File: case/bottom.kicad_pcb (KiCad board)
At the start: 2 copper layers, 135 x 93.7 mm, 5 parts

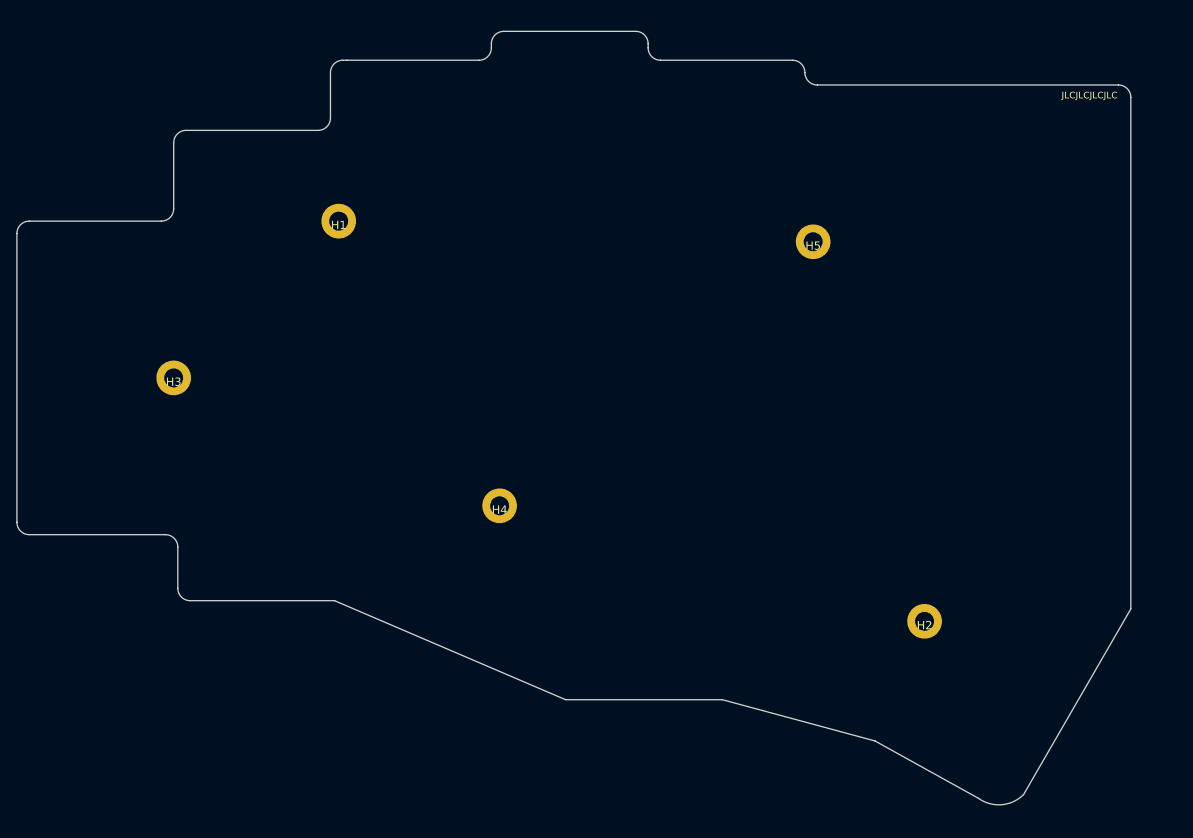
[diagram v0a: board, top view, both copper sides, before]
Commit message: update breakaway design to satisfy jlcpcb
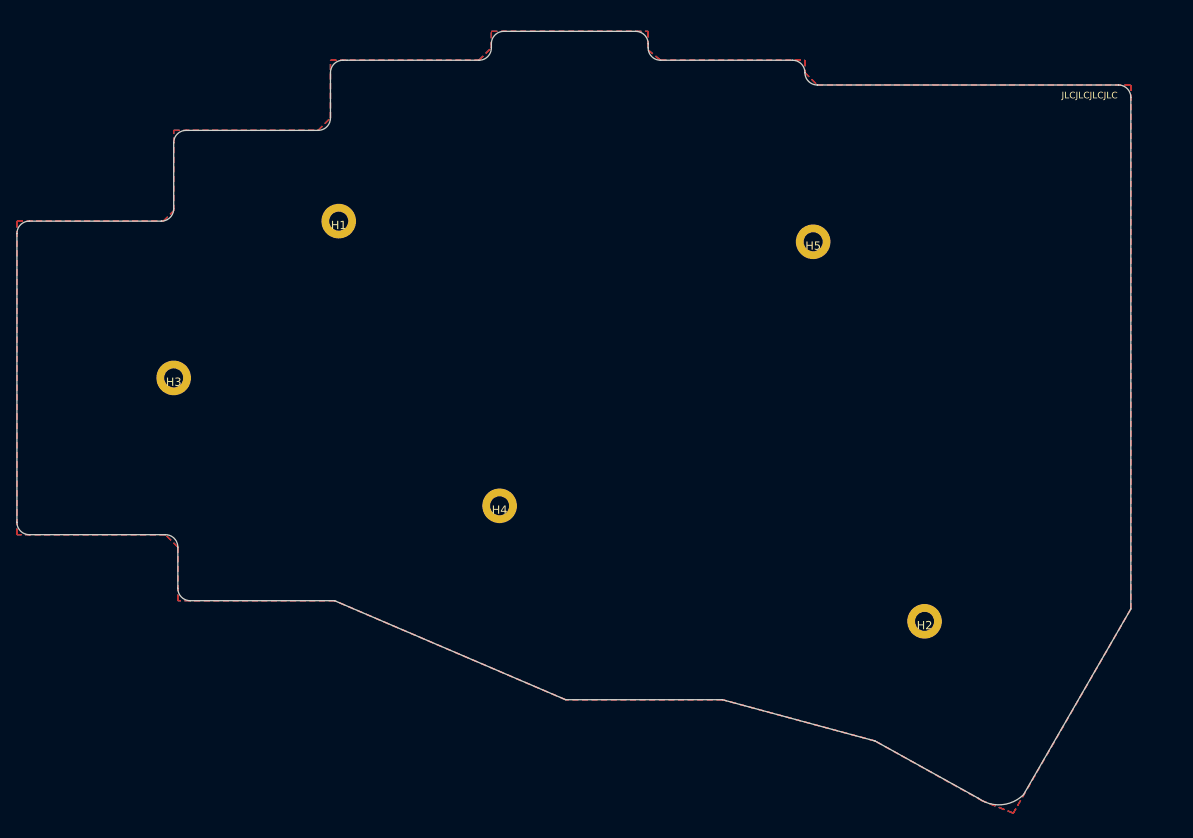
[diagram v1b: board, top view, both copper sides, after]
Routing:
- added copper zone on B.Cu, net (none)
- added copper zone on F.Cu, net (none)
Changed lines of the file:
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@@
     (effects (font (size 0.8 0.8) (thickness 0.15)))
   )
+  (zone (net 0) (net_name "") (layers F&B.Cu) (hatch edge 0.508)
+    (connect_pads (clearance 0.508))
+    (min_thickness 0.254) (filled_areas_thickness no)
+    (fill yes (thermal_gap 0.508) (thermal_bridge_width 0.508))
+    (polygon
+      (pts
+        (xy 145 53.75)
+        (xy 146.5 55)
+        (xy 164 55)
+        (xy 164 56.5)
+        (xy 165.5 58)
+        (xy 203.5 58)
+        (xy 203.5 121.5)
+        (xy 189.25 146.25)
+        (xy 185.5 144.75)
+        (xy 172.5 137.5)
+        (xy 154 132.5)
+        (xy 135 132.5)
+        (xy 107 120.5)
+        (xy 88 120.5)
+        (xy 88 114)
+        (xy 86.5 112.5)
+        (xy 68.5 112.5)
+        (xy 68.5 74.5)
+        (xy 86.25 74.5)
+        (xy 87.5 73.25)
+        (xy 87.5 63.5)
+        (xy 105 63.5)
+        (xy 106.5 62)
+        (xy 106.5 55)
+        (xy 124.5 55)
+        (xy 126 53.5)
+        (xy 126 51.5)
+        (xy 145 51.5)
+      )
+    )
+  )
+  (zone (net 0) (net_name "") (layer "F.Cu") (hatch edge 0.508)
+    (connect_pads (clearance 0.508))
+    (min_thickness 0.254) (filled_areas_thickness no)
+    (fill yes (thermal_gap 0.508) (thermal_bridge_width 0.508))
+    (polygon
+      (pts
+        (xy 145 53.75)
+        (xy 146.5 55)
+        (xy 164 55)
+        (xy 164 56.5)
+        (xy 165.5 58)
+        (xy 203.5 58)
+        (xy 203.5 121.5)
+        (xy 189.466207 145.874483)
+        (xy 189.25 146.25)
+        (xy 185.5 144.75)
+        (xy 172.5 137.5)
+        (xy 154 132.5)
+        (xy 135 132.5)
+        (xy 107 120.5)
+        (xy 88 120.5)
+        (xy 88 114)
+        (xy 86.5 112.5)
+        (xy 68.5 112.5)
+        (xy 68.5 74.5)
+        (xy 86.25 74.5)
+        (xy 87.5 73.25)
+        (xy 87.5 63.5)
+        (xy 105 63.5)
+        (xy 106.5 62)
+        (xy 106.5 55)
+        (xy 124.5 55)
+        (xy 126 53.5)
+        (xy 126 51.5)
+        (xy 145 51.5)
+      )
+    )
+  )
 )

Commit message: update case files
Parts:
- moved H1 1.46 mm to (108.2, 73.2)
- moved H2 1.46 mm to (179.2, 121.8)
- moved H3 1.46 mm to (88.2, 92.2)
- moved H4 1.46 mm to (127.8, 107.8)
- moved H5 1.46 mm to (165.8, 75.8)
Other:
- board size 135 x 93.7 mm -> 135 x 95.7 mm

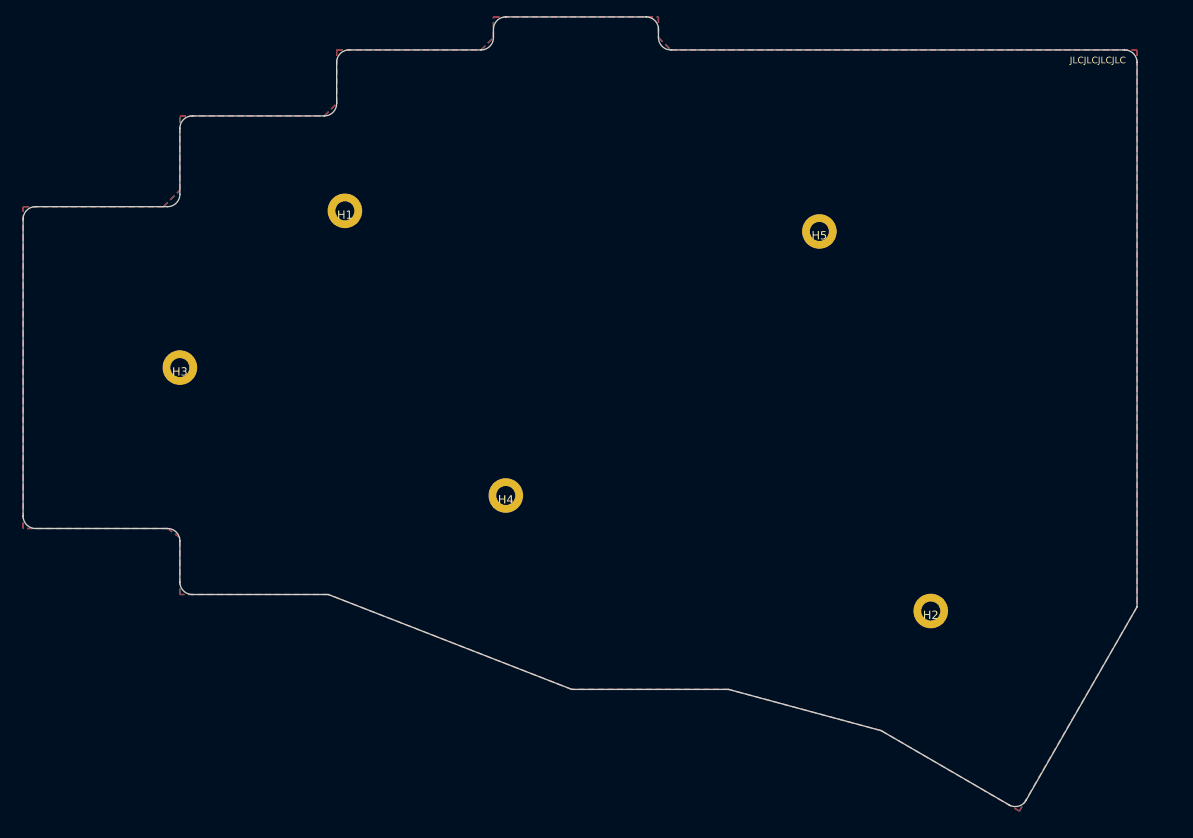
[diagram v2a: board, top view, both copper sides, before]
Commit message: update cases, extra hole on right side
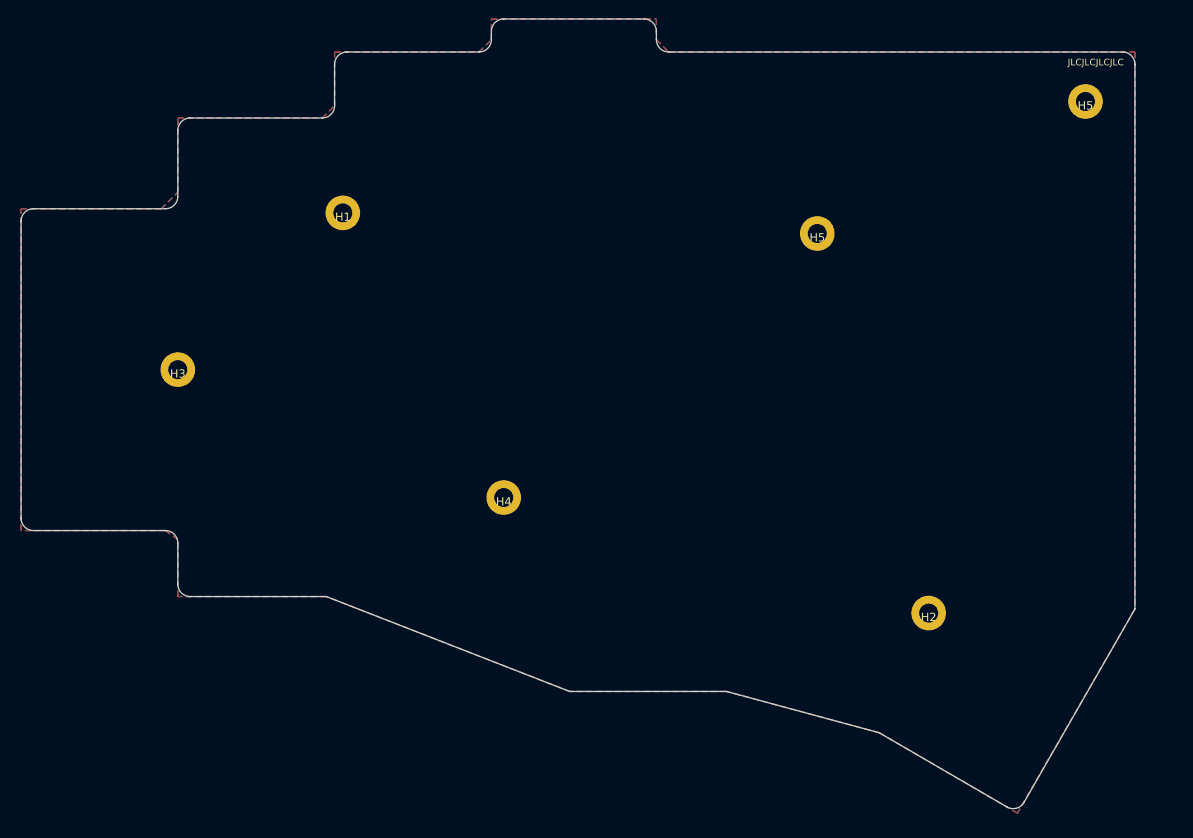
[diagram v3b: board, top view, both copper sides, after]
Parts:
- added H5: MountingHole, kbd:M2_Hole_TH, F.Cu at (198.0, 60.0)
- moved H1 0.35 mm to (108.0, 73.5)
- moved H2 0.35 mm to (179.0, 122.0)
- moved H3 0.35 mm to (88.0, 92.5)
- moved H4 0.35 mm to (127.5, 108.0)
- moved H5 0.35 mm to (165.5, 76.0)
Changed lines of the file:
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@@
       (layerselection 0x00010fc_ffffffff)
       (disableapertmacros false)
-      (usegerberextensions false)
+      (usegerberextensions true)
       (usegerberattributes true)
-      (usegerberadvancedattributes true)
+      (usegerberadvancedattributes false)
       (creategerberjobfile false)
       (svguseinch false)
@@
       (psa4output false)
       (plotreference true)
-      (plotvalue true)
+      (plotvalue false)
       (plotinvisibletext false)
       (sketchpadsonfab false)
-      (subtractmaskfromsilk false)
+      (subtractmaskfromsilk true)
       (outputformat 1)
       (mirror false)
@@
   (net 0 "")
   (footprint "kbd:M2_Hole_TH" (layer "F.Cu")
-    (at 127.75 107.75)
+    (at 127.5 108)
     (property "Sheetfile" "pica40.kicad_sch")
     (property "Sheetname" "")
@@
   )
   (footprint "kbd:M2_Hole_TH" (layer "F.Cu")
-    (at 179.25 121.75)
+    (at 179 122)
     (property "Sheetfile" "pica40.kicad_sch")
     (property "Sheetname" "")
@@
   )
   (footprint "kbd:M2_Hole_TH" (layer "F.Cu")
-    (at 88.25 92.25)
+    (at 198 60)
+    (property "Sheetfile" "pica40.kicad_sch")
+    (property "Sheetname" "")
+    (attr through_hole)
+    (fp_text reference "H5" (at 0 0.5) (layer "F.SilkS")
+      (effects (font (size 1 1) (thickness 0.15)))
+    )
+    (fp_text value "MountingHole" (at 0 -0.5) (layer "F.Fab")
+      (effects (font (size 1 1) (thickness 0.15)))
+    )
+    (pad "" thru_hole circle locked (at 0 0) (size 4.2 4.2) (drill 2.3) (layers *.Cu *.Mask))
+  )
+  (footprint "kbd:M2_Hole_TH" (layer "F.Cu")
+    (at 88 92.5)
     (property "Sheetfile" "pica40.kicad_sch")
     (property "Sheetname" "")
@@
   )
   (footprint "kbd:M2_Hole_TH" (layer "F.Cu")
-    (at 165.75 75.75)
+    (at 165.5 76)
     (property "Sheetfile" "pica40.kicad_sch")
     (property "Sheetname" "")
@@
   )
   (footprint "kbd:M2_Hole_TH" (layer "F.Cu")
-    (at 108.25 73.25)
+    (at 108 73.5)
     (property "Sheetfile" "pica40.kicad_sch")
     (property "Sheetname" "")
@@
     (pad "" thru_hole circle locked (at 0 0) (size 4.2 4.2) (drill 2.3) (layers *.Cu *.Mask))
   )
-  (gr_arc (start 147.75 53.75) (mid 146.68934 53.31066) (end 146.25 52.25) (layer "Edge.Cuts") (width 0.1))
-  (gr_arc (start 107.25 55.25) (mid 107.68934 54.18934) (end 108.75 53.75) (layer "Edge.Cuts") (width 0.1))
-  (gr_line (start 89.75 119.75) (end 106.25 119.75) (layer "Edge.Cuts") (width 0.1))
-  (gr_arc (start 89.75 119.75) (mid 88.68934 119.31066) (end 88.25 118.25) (layer "Edge.Cuts") (width 0.1))
-  (gr_line (start 70.75 111.75) (end 86.75 111.75) (layer "Edge.Cuts") (width 0.1))
-  (gr_arc (start 126.25 51.25) (mid 126.68934 50.18934) (end 127.75 49.75) (layer "Edge.Cuts") (width 0.1))
-  (gr_line (start 124.75 53.75) (end 108.75 53.75) (layer "Edge.Cuts") (width 0.1))
-  (gr_arc (start 88.25 71.25) (mid 87.81066 72.31066) (end 86.75 72.75) (layer "Edge.Cuts") (width 0.1))
-  (gr_line (start 106.25 119.75) (end 135.75 131.25) (layer "Edge.Cuts") (width 0.1))
-  (gr_line (start 204.25 121.25) (end 204.25 55.25) (layer "Edge.Cuts") (width 0.1))
-  (gr_line (start 202.75 53.75) (end 147.75 53.75) (layer "Edge.Cuts") (width 0.1))
-  (gr_arc (start 144.75 49.75) (mid 145.81066 50.18934) (end 146.25 51.25) (layer "Edge.Cuts") (width 0.1))
-  (gr_arc (start 202.75 53.75) (mid 203.81066 54.18934) (end 204.25 55.25) (layer "Edge.Cuts") (width 0.1))
-  (gr_arc (start 69.25 74.25) (mid 69.68934 73.18934) (end 70.75 72.75) (layer "Edge.Cuts") (width 0.1))
-  (gr_arc (start 107.25 60.25) (mid 106.81066 61.31066) (end 105.75 61.75) (layer "Edge.Cuts") (width 0.1))
-  (gr_line (start 135.75 131.25) (end 154.75 131.25) (layer "Edge.Cuts") (width 0.1))
-  (gr_line (start 146.25 52.25) (end 146.25 51.25) (layer "Edge.Cuts") (width 0.1))
-  (gr_line (start 88.25 113.25) (end 88.25 118.25) (layer "Edge.Cuts") (width 0.1))
-  (gr_line (start 107.25 55.25) (end 107.25 60.25) (layer "Edge.Cuts") (width 0.1))
-  (gr_line (start 144.75 49.75) (end 127.75 49.75) (layer "Edge.Cuts") (width 0.1))
-  (gr_line (start 190.799038 144.700962) (end 204.25 121.25) (layer "Edge.Cuts") (width 0.1))
-  (gr_arc (start 88.25 63.25) (mid 88.68934 62.18934) (end 89.75 61.75) (layer "Edge.Cuts") (width 0.1))
-  (gr_arc (start 126.25 52.25) (mid 125.81066 53.31066) (end 124.75 53.75) (layer "Edge.Cuts") (width 0.1))
-  (gr_line (start 69.25 74.25) (end 69.25 110.25) (layer "Edge.Cuts") (width 0.1))
-  (gr_line (start 188.75 145.25) (end 173.25 136.25) (layer "Edge.Cuts") (width 0.1))
-  (gr_line (start 88.25 63.25) (end 88.25 71.25) (layer "Edge.Cuts") (width 0.1))
-  (gr_line (start 126.25 51.25) (end 126.25 52.25) (layer "Edge.Cuts") (width 0.1))
-  (gr_line (start 86.75 72.75) (end 70.75 72.75) (layer "Edge.Cuts") (width 0.1))
-  (gr_line (start 154.75 131.25) (end 173.25 136.25) (layer "Edge.Cuts") (width 0.1))
-  (gr_arc (start 190.799038 144.700962) (mid 189.888233 145.399868) (end 188.75 145.25) (layer "Edge.Cuts") (width 0.1))
-  (gr_line (start 105.75 61.75) (end 89.75 61.75) (layer "Edge.Cuts") (width 0.1))
-  (gr_arc (start 86.75 111.75) (mid 87.81066 112.18934) (end 88.25 113.25) (layer "Edge.Cuts") (width 0.1))
-  (gr_arc (start 70.75 111.75) (mid 69.68934 111.31066) (end 69.25 110.25) (layer "Edge.Cuts") (width 0.1))
-  (gr_text "JLCJLCJLCJLC" (at 199.5 55) (layer "F.SilkS")
+  (gr_arc (start 147.5 54) (mid 146.43934 53.56066) (end 146 52.5) (layer "Edge.Cuts") (width 0.1))
+  (gr_arc (start 107 55.5) (mid 107.43934 54.43934) (end 108.5 54) (layer "Edge.Cuts") (width 0.1))
+  (gr_line (start 89.5 120) (end 106 120) (layer "Edge.Cuts") (width 0.1))
+  (gr_arc (start 89.5 120) (mid 88.43934 119.56066) (end 88 118.5) (layer "Edge.Cuts") (width 0.1))
+  (gr_line (start 70.5 112) (end 86.5 112) (layer "Edge.Cuts") (width 0.1))
+  (gr_arc (start 126 51.5) (mid 126.43934 50.43934) (end 127.5 50) (layer "Edge.Cuts") (width 0.1))
+  (gr_line (start 124.5 54) (end 108.5 54) (layer "Edge.Cuts") (width 0.1))
+  (gr_arc (start 88 71.5) (mid 87.56066 72.56066) (end 86.5 73) (layer "Edge.Cuts") (width 0.1))
+  (gr_line (start 106 120) (end 135.5 131.5) (layer "Edge.Cuts") (width 0.1))
+  (gr_line (start 204 121.5) (end 204 55.5) (layer "Edge.Cuts") (width 0.1))
+  (gr_line (start 202.5 54) (end 147.5 54) (layer "Edge.Cuts") (width 0.1))
+  (gr_arc (start 144.5 50) (mid 145.56066 50.43934) (end 146 51.5) (layer "Edge.Cuts") (width 0.1))
+  (gr_arc (start 202.5 54) (mid 203.56066 54.43934) (end 204 55.5) (layer "Edge.Cuts") (width 0.1))
+  (gr_arc (start 69 74.5) (mid 69.43934 73.43934) (end 70.5 73) (layer "Edge.Cuts") (width 0.1))
+  (gr_arc (start 107 60.5) (mid 106.56066 61.56066) (end 105.5 62) (layer "Edge.Cuts") (width 0.1))
+  (gr_line (start 135.5 131.5) (end 154.5 131.5) (layer "Edge.Cuts") (width 0.1))
+  (gr_line (start 146 52.5) (end 146 51.5) (layer "Edge.Cuts") (width 0.1))
+  (gr_line (start 88 113.5) (end 88 118.5) (layer "Edge.Cuts") (width 0.1))
+  (gr_line (start 107 55.5) (end 107 60.5) (layer "Edge.Cuts") (width 0.1))
+  (gr_line (start 144.5 50) (end 127.5 50) (layer "Edge.Cuts") (width 0.1))
+  (gr_line (start 190.549038 144.950962) (end 204 121.5) (layer "Edge.Cuts") (width 0.1))
+  (gr_arc (start 88 63.5) (mid 88.43934 62.43934) (end 89.5 62) (layer "Edge.Cuts") (width 0.1))
+  (gr_arc (start 126 52.5) (mid 125.56066 53.56066) (end 124.5 54) (layer "Edge.Cuts") (width 0.1))
+  (gr_line (start 69 74.5) (end 69 110.5) (layer "Edge.Cuts") (width 0.1))
+  (gr_line (start 188.5 145.5) (end 173 136.5) (layer "Edge.Cuts") (width 0.1))
+  (gr_line (start 88 63.5) (end 88 71.5) (layer "Edge.Cuts") (width 0.1))
+  (gr_line (start 126 51.5) (end 126 52.5) (layer "Edge.Cuts") (width 0.1))
+  (gr_line (start 86.5 73) (end 70.5 73) (layer "Edge.Cuts") (width 0.1))
+  (gr_line (start 154.5 131.5) (end 173 136.5) (layer "Edge.Cuts") (width 0.1))
+  (gr_arc (start 190.549038 144.950962) (mid 189.63823 145.649869) (end 188.5 145.5) (layer "Edge.Cuts") (width 0.1))
+  (gr_line (start 105.5 62) (end 89.5 62) (layer "Edge.Cuts") (width 0.1))
+  (gr_arc (start 86.5 112) (mid 87.56066 112.43934) (end 88 113.5) (layer "Edge.Cuts") (width 0.1))
+  (gr_arc (start 70.5 112) (mid 69.43934 111.56066) (end 69 110.5) (layer "Edge.Cuts") (width 0.1))
+  (gr_text "JLCJLCJLCJLC" (at 199.25 55.25) (layer "F.SilkS")
     (effects (font (size 0.8 0.8) (thickness 0.15)))
   )
@@
     (polygon
       (pts
-        (xy 146.25 52.25)
-        (xy 147.75 53.75)
-        (xy 204.25 53.75)
-        (xy 204.25 121.25)
-        (xy 190 146)
-        (xy 173.25 136.25)
-        (xy 154.75 131.25)
-        (xy 135.75 131.25)
-        (xy 106.25 119.75)
-        (xy 88.25 119.75)
-        (xy 88.25 112.85)
-        (xy 86.75 111.75)
-        (xy 69.25 111.75)
-        (xy 69.25 72.75)
-        (xy 86.25 72.75)
-        (xy 88.25 70.75)
-        (xy 88.25 61.75)
-        (xy 105.75 61.75)
-        (xy 107.25 60.25)
-        (xy 107.25 53.75)
-        (xy 124.75 53.75)
-        (xy 126.25 52.25)
-        (xy 126.25 49.75)
-        (xy 146.25 49.75)
+        (xy 146 52.5)
+        (xy 147.5 54)
+        (xy 204 54)
+        (xy 204 121.5)
+        (xy 189.75 146.25)
+        (xy 173 136.5)
+        (xy 154.5 131.5)
+        (xy 135.5 131.5)
+        (xy 106 120)
+        (xy 88 120)
+        (xy 88 113.1)
+        (xy 86.5 112)
+        (xy 69 112)
+        (xy 69 73)
+        (xy 86 73)
+        (xy 88 71)
+        (xy 88 62)
+        (xy 105.5 62)
+        (xy 107 60.5)
+        (xy 107 54)
+        (xy 124.5 54)
+        (xy 126 52.5)
+        (xy 126 50)
+        (xy 146 50)
       )
     )

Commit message: update case files
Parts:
- removed the H5 at (198.0, 60.0)
- removed the H5 at (165.5, 76.0)
- added G***: LOGO, pica:logo, F.Cu at (195.5, 68.5)
- added G***: LOGO, pica:logo, B.Cu at (198.0, 69.0)
- added H5: MountingHole, kbd:thread_m2, F.Cu at (169.5, 77.1)
- added H6: MountingHole, kbd:thread_m2, F.Cu at (192.0, 84.1)
- added H7: MountingHole, kbd:thread_m2, F.Cu at (200.8, 84.1)
- H1, H2, H3, H4: footprint kbd:M2_Hole_TH -> kbd:thread_m2
- moved H3 8.75 mm to (90.8, 100.8), turned to 5 degrees
- moved H2 4.14 mm to (183.0, 123.1)
- moved H4 4.14 mm to (131.5, 109.1)
- moved H1 2.53 mm to (110.3, 74.6)
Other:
- board size 135 x 95.7 mm -> 137.8 x 95.7 mm
- board text added: "Pica40 v2"
- board text added: "github.com/zzeneg/pica40"
